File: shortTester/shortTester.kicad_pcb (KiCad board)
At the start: 2 copper layers, 127 x 104 mm, 28 parts, among them J2 Conn_02x38_Counter_Clockwise, M2 MountingHole_2.2mm_M2, U1 CD74HC4067M, U10 CD74HC4067M, U11 CD74HC4067M, U2 Pico, U3 CD74HC4067M, U4 CD74HC4067M, U5 CD74HC4067M, U6 CD74HC4067M, U7 CD74HC4067M, U8 CD74HC4067M, U9 CD74HC4067M

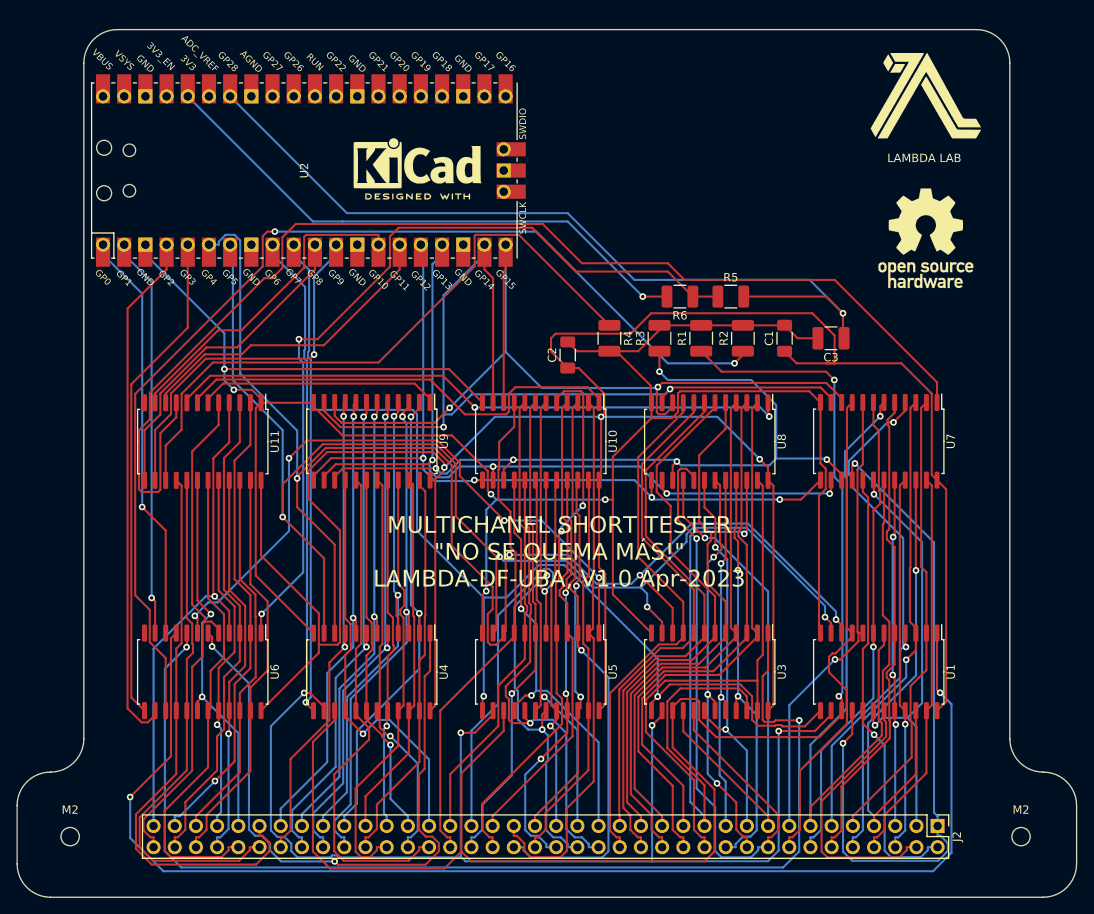
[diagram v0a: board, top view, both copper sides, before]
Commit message: Fixed missing tracks. Simplified MUx GND. Added software.
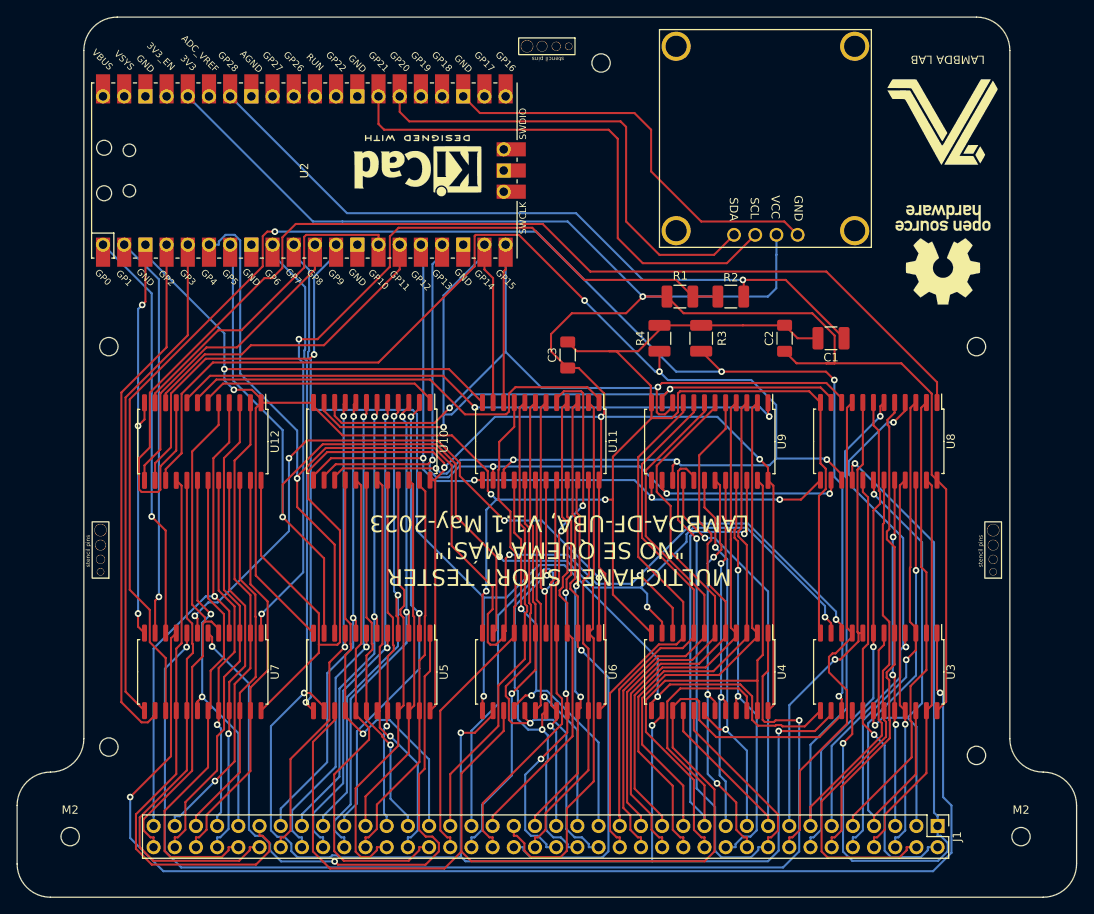
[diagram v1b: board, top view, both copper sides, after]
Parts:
- removed the R2 at (171.0, 72.0)
- removed the R4 at (155.0, 72.0)
- added G***: LOGO, skLib:shortQR, B.Cu at (174.0, 48.0)
- added M2: MountingHole_2.2mm_M2, MountingHole:MountingHole_2.2mm_M2, F.Cu at (95.0, 121.0)
- added M2: MountingHole_2.2mm_M2, MountingHole:MountingHole_2.2mm_M2, F.Cu at (95.0, 73.0)
- added M2: MountingHole_2.2mm_M2, MountingHole:MountingHole_2.2mm_M2, F.Cu at (154.0, 39.0)
- added M2: MountingHole_2.2mm_M2, MountingHole:MountingHole_2.2mm_M2, F.Cu at (199.0, 73.0)
- added M2: MountingHole_2.2mm_M2, MountingHole:MountingHole_2.2mm_M2, F.Cu at (199.0, 122.0)
- added REF**: stencil pins, skLib:alignment_pins, F.Cu at (201.0, 98.5)
- added REF**: stencil pins, skLib:alignment_pins, F.Cu at (148.6, 37.0)
- added REF**: stencil pins, skLib:alignment_pins, F.Cu at (94.0, 98.5)
- added U1: SSD1306, skLib:SSD1306, F.Cu at (177.6, 59.6)
- moved G*** 3.91 mm to (195.5, 46.0), turned to 0 degrees
- moved G*** 3.68 mm to (195.0, 46.0), turned to 180 degrees
- moved REF** 2.89 mm to (195.0, 62.0), turned to 180 degrees
- moved REF** 1.00 mm to (132.0, 52.0), turned to 180 degrees
- moved REF** 1.00 mm to (132.0, 52.0), turned to 0 degrees
- renumbered C3 to C1, C1 to C2, C2 to C3, J2 to J1, R6 to R1, R5 to R2, R1 to R3, R3 to R4, U9 to U10, U10 to U11, U11 to U12, U1 to U3, U3 to U4, U4 to U5, U5 to U6, U6 to U7, U7 to U8, U8 to U9
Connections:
- R1 pad 2: VDD -> VCC
- R3 pad 1: /mux_block_A/en2 -> /mux_block_A/en
- R4 pad 1: /mux_block_B/en2 -> /mux_block_B/en
- U10 pad 15: /mux_block_B/en2 -> /mux_block_B/en
- U11 pad 15: /mux_block_B/en2 -> /mux_block_B/en
- U12 pad 12: unconnected-(U11-GND-Pad12) -> COMB
- U12 pad 15: /mux_block_B/en1 -> /mux_block_B/en
- U2 pad 23: unconnected-(U2-GND-Pad23) -> GND_B
- U2 pad 26: unconnected-(U2-GPIO20-Pad26) -> SDA0
- U2 pad 27: unconnected-(U2-GPIO21-Pad27) -> SCL0
- U2 pad 36: VDD -> VCC
- U3 pad 15: /mux_block_A/en2 -> /mux_block_A/en
- U4 pad 15: /mux_block_A/en2 -> /mux_block_A/en
- U5 pad 15: /mux_block_A/en2 -> /mux_block_A/en
- U6 pad 15: /mux_block_A/en2 -> /mux_block_A/en
- U7 pad 12: unconnected-(U6-GND-Pad12) -> COMB
- U7 pad 15: /mux_block_A/en1 -> /mux_block_A/en
- U8 pad 15: /mux_block_B/en2 -> /mux_block_B/en
- U9 pad 15: /mux_block_B/en2 -> /mux_block_B/en
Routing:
- net /mux_block_A/en: track 0.00 -> 317.7 mm, vias 0 -> 4
- net /mux_block_A/en2: track 190.3 -> 0.00 mm, vias 2 -> 0
- net /mux_block_B/en: track 0.00 -> 179.8 mm, vias 0 -> 6
- net /mux_block_A/en1: track 129.9 -> 0.00 mm, vias 2 -> 0
- net /mux_block_B/en2: track 94.5 -> 0.00 mm, vias 5 -> 0
- net VCC: track 328.9 -> 418.3 mm, vias 3 -> 4
- net /mux_block_B/en1: track 77.0 -> 0.00 mm
- net VDD: track 67.4 -> 0.00 mm, vias 1 -> 0
- net SCL0: track 0.00 -> 63.8 mm
- net SDA0: track 0.00 -> 56.7 mm
- net COMB: track 279.3 -> 329.7 mm, vias 5 -> 8
- net GND_B: track 0.00 -> 49.9 mm
- net Net-(U2-GPIO28_ADC2): track 100.0 -> 87.6 mm
- net SA12: track 62.4 -> 63.0 mm
- net SA13: track 59.3 -> 59.9 mm
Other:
- board size 127 x 104 mm -> 127 x 105.5 mm
- board text added: "MULTICHANEL SHORT TESTER {dblquote}NO SE QUEMA MÁS!{dblquote} LAMBDA-DF-UBA, V1.1 May-2023"
- board text removed: "MULTICHANEL SHORT TESTER {dblquote}NO SE QUEMA MÁS!{dblquote} LAMBDA-DF-UBA, V1.0 Apr-2023"
